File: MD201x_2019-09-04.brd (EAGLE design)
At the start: 80 x 50 mm, 103 parts, among them IC1 78L05F, IC2 LM321MF, J1 8P8C-LED, J10 1744446-4, J2 1744446-4, J3 XH-4-SIDE, J4 MA04-2, J5 MA05-2, J6 MA02-2, Q1 N-MOSFET-, Q2 N-MOSFET-, Q3 N-MOSFET-, Q4 N-MOSFET-, Q5 BSS123, U1 STM32F103C8, U10 XC6206, U2 NCV7351D1E, U3 SI8621AB-B-IS, U4 TLP184, U5 NCP5106D, U6 NCP5106D, U7 NCS199, U8 7815DT, U9 7805DT, X1 CSTCE8M00G55

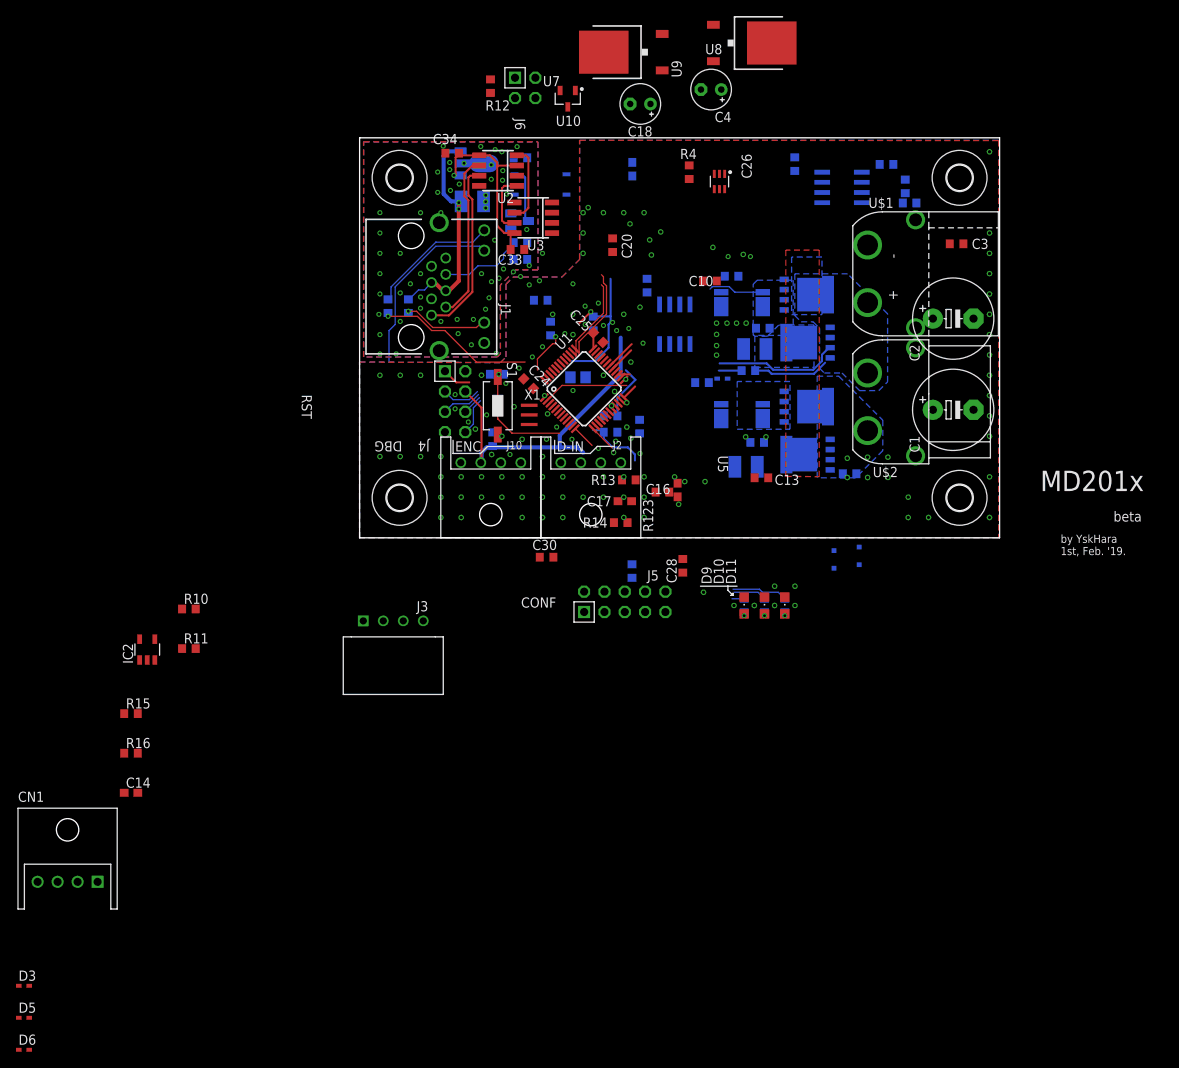
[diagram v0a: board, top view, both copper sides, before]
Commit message: エンコーダとand回路周りの修正
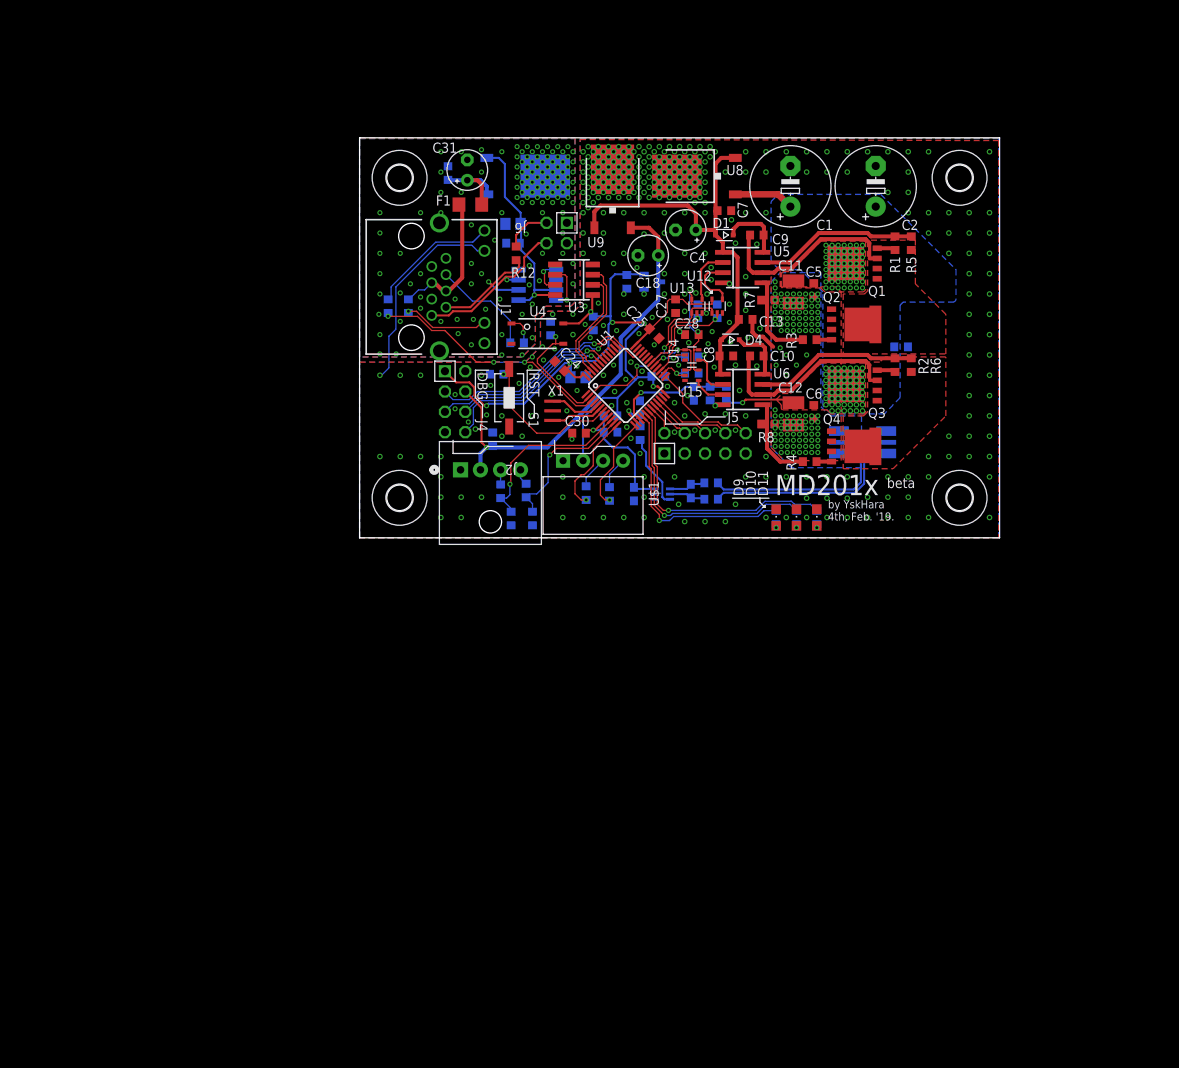
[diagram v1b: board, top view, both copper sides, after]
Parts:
- removed CN1: (no value), jst-xa:S4B-XASK-1
- removed D2, D3, D5, D6: (no value), diode:SOD523
- removed IC1: 78L05F, linear:SOT89
- removed IC2: LM321MF, linear:SOT23-5
- removed J10: 1744446-4, con-ep25:1744446-4
- removed J3: XH-4-SIDE, con-xh:CON-XH-4-SIDE
- removed Q5: BSS123, transistor-small-signal:SOT23
- removed U$2: XT60PW-F, lib_ysk:XT60PW-F
- added C31: 22u, rcl:E2,5-5
- added C32: 100n, rcl:C0603
- added C35: 220p, rcl:C0603
- added F1: (no value), rcl:R1206
- added R22, R23: 100k, rcl:R0603
- added R24: 100R, rcl:R0603
- added U11: 7805DT, linear:TO252
- added U12, U13, U14, U15: 74AHC1G08DCK, 74xx-little-us:SC70-5
- C33: device rcl:C0603 -> rcl:C0805
- C36: value 100n -> 220p; device rcl:C1210 -> rcl:C0603
- C5, C6: value 100n/50V -> (none)
- J2: value 1744446-4 -> 1744426-4; device con-ep25:1744446-4 -> EP2.5:CONN4_1744426-4
- R10, R11: value 10 -> (none)
- R15, R16: value 10 -> 100R
- R17: value 1k -> 100R
- R18: value 47k -> 100k
- R19: value 0.5m -> 100k; device r_shunt:CSS2H-2512 -> rcl:R0603
- U$1: value XT60PW-M -> XH-4-SIDE; device lib_ysk:XT60PW-M -> con-xh:CON-XH-4-SIDE
- moved C14 79.5 mm to (41.4, 5.84), flipped to the bottom, turned to 90 degrees
- moved R11 67.9 mm to (43.9, 4.83), flipped to the bottom
- moved R10 67.2 mm to (43.9, 6.86), flipped to the bottom
- moved R16 59.3 mm to (20.8, 5.92), flipped to the bottom, turned to 90 degrees
- moved R15 53.9 mm to (17.6, 5.82), flipped to the bottom, turned to 90 degrees
- moved D1 43.5 mm to (45.6, 37.8), flipped to the top, turned to 180 degrees
- moved R17 43.5 mm to (31.2, 5.49), turned to 90 degrees
- moved C15 40.6 mm to (34.3, 5.46)
- moved C36 39.9 mm to (18.9, 2.41), turned to 90 degrees
- moved U7 39.7 mm to (37.8, 5.46), flipped to the bottom, turned to 180 degrees
- moved R4 39.2 mm to (56.3, 9.53), turned to 0 degrees
- moved U$1 35.1 mm to (35.4, 11.9), turned to 180 degrees
- moved C1 34.6 mm to (53.8, 43.9), turned to 90 degrees
- moved C27 33.6 mm to (39.5, 29.0), flipped to the top
- moved D4 30.4 mm to (46.4, 24.8), flipped to the top, turned to 180 degrees
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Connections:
- net CANRX_ISO renamed N$27
- net CANTX_ISO renamed N$23
- removed net A_LS: Q2.1, Q2.2, Q2.3, R19.2, R7.1
- removed net B_LS: C6.2, Q4.1, Q4.2, Q4.3, R8.1, R9.2
- removed net DC_ISO: C36.1, IC1.3, J1.4, J1.5, R20.1
- removed net ISENSE_B: C16.2, R123.1
- removed net N$14: IC2.1, R10.2, R11.1
- removed net N$24: IC2.3, IC2.4
- removed net REF: C14.2, R15.2, R16.1, U7.1
- new net 24V_ISO: C31.+, C32.1, F1.1, U11.1
- new net N$15: R17.2, U$1.P$4
- new net N$30: R28.1, U4.1
- new net N$36: C14.2, R10.2, U7.4
- new net N$37: C14.1, R11.2, U7.5
- new net VCS: C11.2, C12.2, C13.2, C5.2, C6.2, Q2.1, Q2.2, Q2.3, Q4.1, Q4.2, Q4.3, R7.1, R8.1, R9.2$1, R9.2$2
- net !EMS: now also U12.1, U13.1, U14.1, U15.1
- net !EMS_ISO: no longer R18.2
- net +3V3: now also U$1.P$2, U12.5, U13.5, U14.5, U15.5
- net +5V: now also J2.2; no longer J10.P2, J3.P$2
- net 3V3A: no longer IC2.5, R10.1, R15.1
- net 5V_ISO: now also U11.2; no longer IC1.1, R17.2
- net A_OUT: no longer U$2.POS
- net B_OUT: no longer U$2.NEG
- net CANH: now also J6.1
- net CANL: now also R12.1
- net ENC_A: now also C36.2, R15.1, U1.10; no longer J10.P3, U1.42
- net ENC_B: now also C35.2, R16.1, U1.11; no longer J10.P4, U1.43
- net GNDA: now also C35.1, C36.1, J2.1, R18.2, R19.2, R22.2, R23.2, R9.1$1, R9.1$2, U12.3, U13.3, U14.3, U15.3, U7.1; no longer C11.2, C12.2, C13.2, C14.1, C5.2, IC2.2, J10.P1, J3.P$1, R11.2, R16.2, R19.1, R9.1, U$1.NEG, U$1.P$2, U$2.P$1, U$2.P$2
- net GNDIO: now also C31.-, C32.2, U11.3, U4.2; no longer C36.2, IC1.2, IC1.2@1, Q5.2, R18.1
- net IN_A: now also R24.1; no longer J3.P$3
- net IN_B: now also R17.1; no longer J3.P$4
- net IN_HI_A: now also U13.4
- net IN_HI_A_PRE: now also R18.1, U13.2
- net IN_HI_B: now also U14.4
- net IN_HI_B_PRE: now also R19.1, U14.2
- net IN_LO_A: now also U12.4
- net IN_LO_A_PRE: now also R22.1, U12.2
- net IN_LO_B: now also U15.4
- net IN_LO_B_PRE: now also R23.1, U15.2
- net ISENSE: now also C16.2, R123.1
- net N$1: no longer D6.C
- net N$11: no longer D5.C
- net N$12: now also J2.4, R16.2; no longer D2.A, Q3.4, R2.2
- net N$13: now also Q3.4, R2.2; no longer J6.1
- net N$16: now also J2.3, R15.2; no longer R17.1, U4.1
- net N$17: now also R24.2, U$1.P$3; no longer Q5.3, U4.2
- net N$2: no longer D2.C
- net N$4: no longer D6.A
- net N$5: no longer D3.C
- net N$61: no longer D5.A
- net N$64: no longer D3.A
- net N$8: now also F1.2, J1.4, J1.5, R20.1; no longer Q5.1, R28.1
- net UART_RX: now also U1.43
- net UART_TX: now also U1.42
- net VCC: no longer U$1.POS
- net VCS_B_N: now also R11.1; no longer U7.5
- net VCS_B_P: now also R10.1; no longer U7.4
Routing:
- net +3V3: track 34.6 -> 118.5 mm, vias 2 -> 8
- net +15V: track 0.00 -> 53.6 mm
- net !EMS: track 16.8 -> 45.0 mm, vias 1 -> 4
- net DC_ISO: track 27.6 -> 0.00 mm, vias 2 -> 0
- net LED0: track 1.52 -> 28.9 mm, vias 0 -> 1
- net LED1: track 4.14 -> 31.1 mm, vias 0 -> 1
- net VCS_B_N: track 0.00 -> 26.8 mm
- net LED2: track 6.97 -> 33.3 mm, vias 0 -> 1
- net SWDIO: track 4.91 -> 29.5 mm, vias 0 -> 1
- net A_OUT: track 0.00 -> 24.5 mm
- net ENC_A: track 0.00 -> 22.4 mm, vias 0 -> 1
- net SWCLK: track 5.09 -> 25.9 mm, vias 0 -> 1
- net N$1: track 0.00 -> 20.3 mm
- net VCS_B_P: track 7.01 -> 26.1 mm
- net ENC_B: track 0.00 -> 18.9 mm, vias 0 -> 1
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- added copper zone on layer 1, net A_OUT
- added copper zone on layer 1, net B_OUT
- added copper zone on layer 1, net VCS
- added copper zone on layer 16, net VCS
- removed copper zone on layer 16, net A_LS
- removed copper zone on layer 16, net A_OUT
- removed copper zone on layer 16, net B_LS
- removed copper zone on layer 16, net B_OUT
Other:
- board text added: "0"
- board text added: "1"
- board text added: "2"
- board text added: "3"
- board text added: "4"
- board text added: "B1"
- board text added: "C1"
- board text added: "C10"
- board text added: "C11"
- board text added: "C12"
- board text added: "C13"
- board text added: "C14"
- board text added: "C15"
- board text added: "C16"
- board text added: "C17"
- board text added: "C18"
- board text added: "C19"
- board text added: "C2"
- board text added: "C20"
- board text added: "C21"
- board text added: "C22"
- board text added: "C23"
- board text added: "C24"
- board text added: "C25"
- board text added: "C26"
- board text added: "C27"
- board text added: "C28"
- board text added: "C29"
- board text added: "C3"
- board text added: "C30"
- board text added: "C31"
- board text added: "C32"
- board text added: "C33"
- board text added: "C34"
- board text added: "C35"
- board text added: "C36"
- board text added: "C4"
- board text added: "C5"
- board text added: "C6"
- board text added: "C7"
- board text added: "C8"
- board text added: "C9"
- board text added: "CAN TERM."
- board text added: "D1"
- board text added: "D10"
- board text added: "D11"
- board text added: "D4"
- board text added: "D9"
- board text added: "F1"
- board text added: "J1"
- board text added: "J4"
- board text added: "J5"
- board text added: "J6"
- board text added: "J7"
- board text added: "OPEN"
- board text added: "Q1"
- board text added: "Q2"
- board text added: "Q3"
- board text added: "Q4"
- board text added: "R1"
- board text added: "R10"
- board text added: "R109"
- board text added: "R11"
- board text added: "R110"
- board text added: "R111"
- board text added: "R12"
- board text added: "R123"
- board text added: "R13"
- board text added: "R14"
- board text added: "R15"
- board text added: "R16"
- board text added: "R17"
- board text added: "R18"
- board text added: "R19"
- board text added: "R2"
- board text added: "R20"
- board text added: "R21"
- board text added: "R22"
- board text added: "R23"
- board text added: "R24"
- board text added: "R28"
- board text added: "R3"
- board text added: "R30"
- board text added: "R4"
- board text added: "R5"
- board text added: "R6"
- board text added: "R7"
- board text added: "R8"
- board text added: "R9"
- board text added: "S1"
- board text added: "TERM"
- board text added: "U$1"
- board text added: "U1"
- board text added: "U10"
- board text added: "U11"
- board text added: "U12"
- board text added: "U13"
- board text added: "U14"
- board text added: "U15"
- board text added: "U2"
- board text added: "U3"
- board text added: "U4"
- board text added: "U5"
- board text added: "U6"
- board text added: "U7"
- board text added: "U8"
- board text added: "U9"
- board text added: "X1"
- board text added: "by YskHara 4th, Feb. '19."
- board text removed: "DIN_A"
- board text removed: "DIN_B"
- board text removed: "ENC_A"
- board text removed: "ENC_B"
- board text removed: "by YskHara 1st, Feb. '19."
